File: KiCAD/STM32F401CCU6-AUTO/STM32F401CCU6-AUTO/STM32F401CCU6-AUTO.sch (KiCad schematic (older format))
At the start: 69 parts

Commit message: add auto
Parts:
- added C?: 470uF/25V, symbol Device:CP
- added C?: 0.1uF, Capacitor_SMD:C_0603_1608Metric_Pad1.05x0.95mm_HandSolder, symbol Device:C_Small
- added J? (x4): Conn_01x02_Male, symbol Connector:Conn_01x02_Male
- added L? (x4): if_amplifier, symbol qmechanics:if_amplifier
- added Q? (x4): S8050, Package_TO_SOT_THT:TO-92_Inline, symbol Transistor_BJT:S8050
- added R? (x8): 10K, Resistor_SMD:R_0402_1005Metric, symbol Device:R
- added R? (x4): 5K6, Resistor_SMD:R_0402_1005Metric, symbol Device:R
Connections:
- net labels added: POWER_IF
- wire segments 234 -> 310
- no-connect marks 20 -> 24

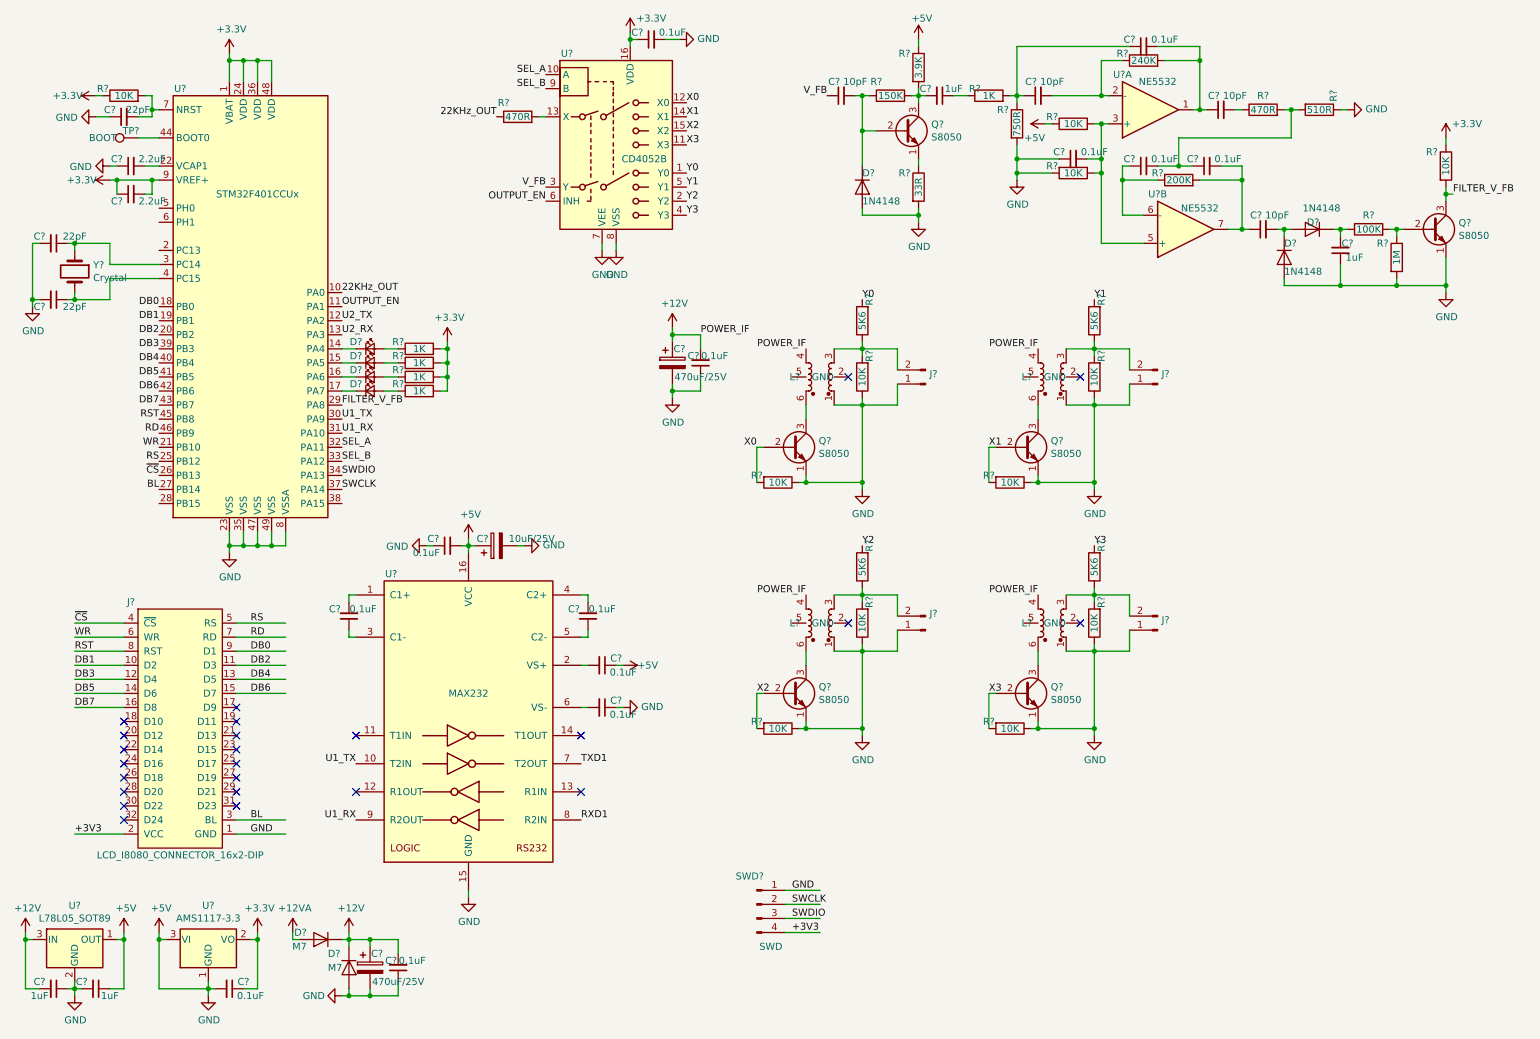
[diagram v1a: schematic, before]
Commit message: 添加DS并完善原理图
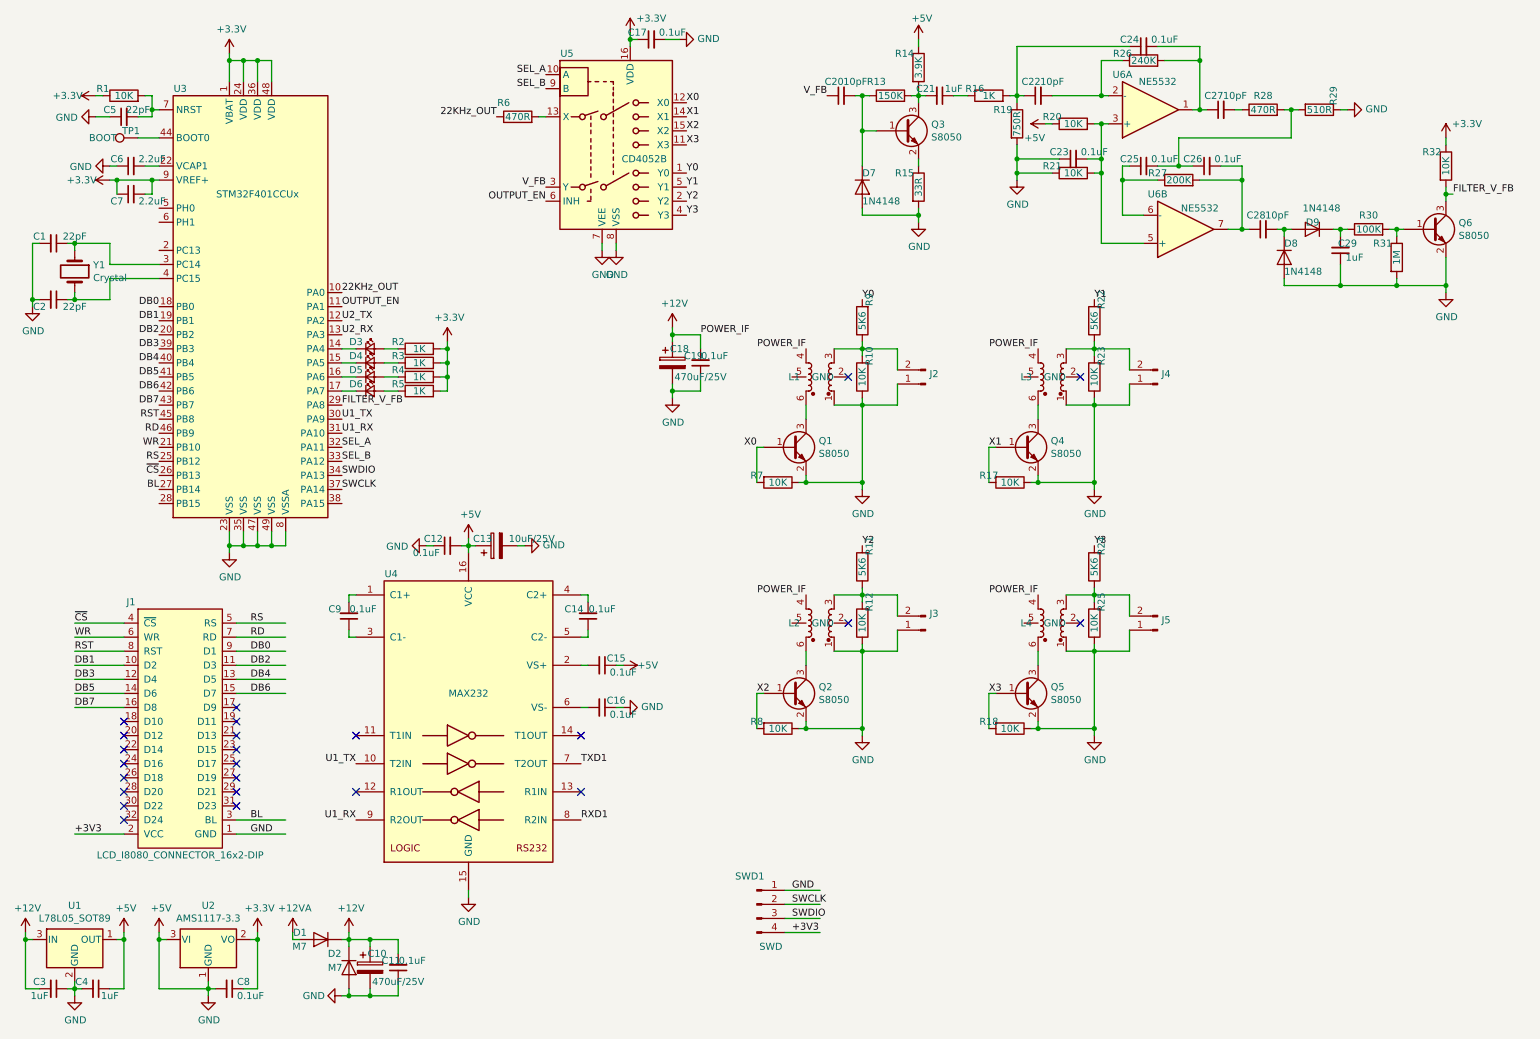
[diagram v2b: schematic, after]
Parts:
- removed Q? (x6): S8050, Package_TO_SOT_THT:TO-92_Inline, symbol Transistor_BJT:S8050
- added Q1, Q2, Q3, Q4, Q5, Q6: S8050, Package_TO_SOT_SMD:SOT-23, symbol Device:Q_NPN_BEC
- C1, C2: renamed from C?; footprint (none) -> Capacitor_SMD:C_0603_1608Metric_Pad1.05x0.95mm_HandSolder
- C10, C13, C18: renamed from C?; footprint (none) -> Capacitor_THT:CP_Radial_D6.3mm_P2.50mm
- C5: renamed from C?; footprint Capacitor_SMD:C_0402_1005Metric -> Capacitor_SMD:C_0603_1608Metric_Pad1.05x0.95mm_HandSolder
- L1, L2, L3, L4: renamed from L?; footprint (none) -> qmechanics:if_amp
- R1, R10, R11, R12, R13, R14, R15, R17, R18, R19, R20, R21, R22, R23, R24, R25, R26, R27, R28, R29, R31, R32, R6, R7, R8, R9: renamed from R?; footprint Resistor_SMD:R_0402_1005Metric -> Resistor_SMD:R_0603_1608Metric_Pad1.05x0.95mm_HandSolder
- TP1: renamed from TP?; footprint (none) -> TestPoint:TestPoint_Loop_D2.50mm_Drill1.85mm
- U4: renamed from U?; footprint (none) -> qchip:MAX232DR-SOIC-16-Pitch1.27mm_Handsoldering
- U5: renamed from U?; footprint (none) -> qchip:CD4052BM96-SOIC-16-Pitch1.27mm
- U6: renamed from U?; footprint (none) -> qchip:NE5532D-SOIC-8_Pitch1.27mm
- Y1: renamed from Y?; footprint (none) -> Crystal:Crystal_SMD_HC49-SD
- gave numbers to parts that had none: 47
